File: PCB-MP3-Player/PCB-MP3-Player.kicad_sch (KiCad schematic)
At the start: 5 parts, among them J1 Conn_01x02_Pin, J2 PCM5102A, J3 Oled, J4 Conn_01x06_Pin

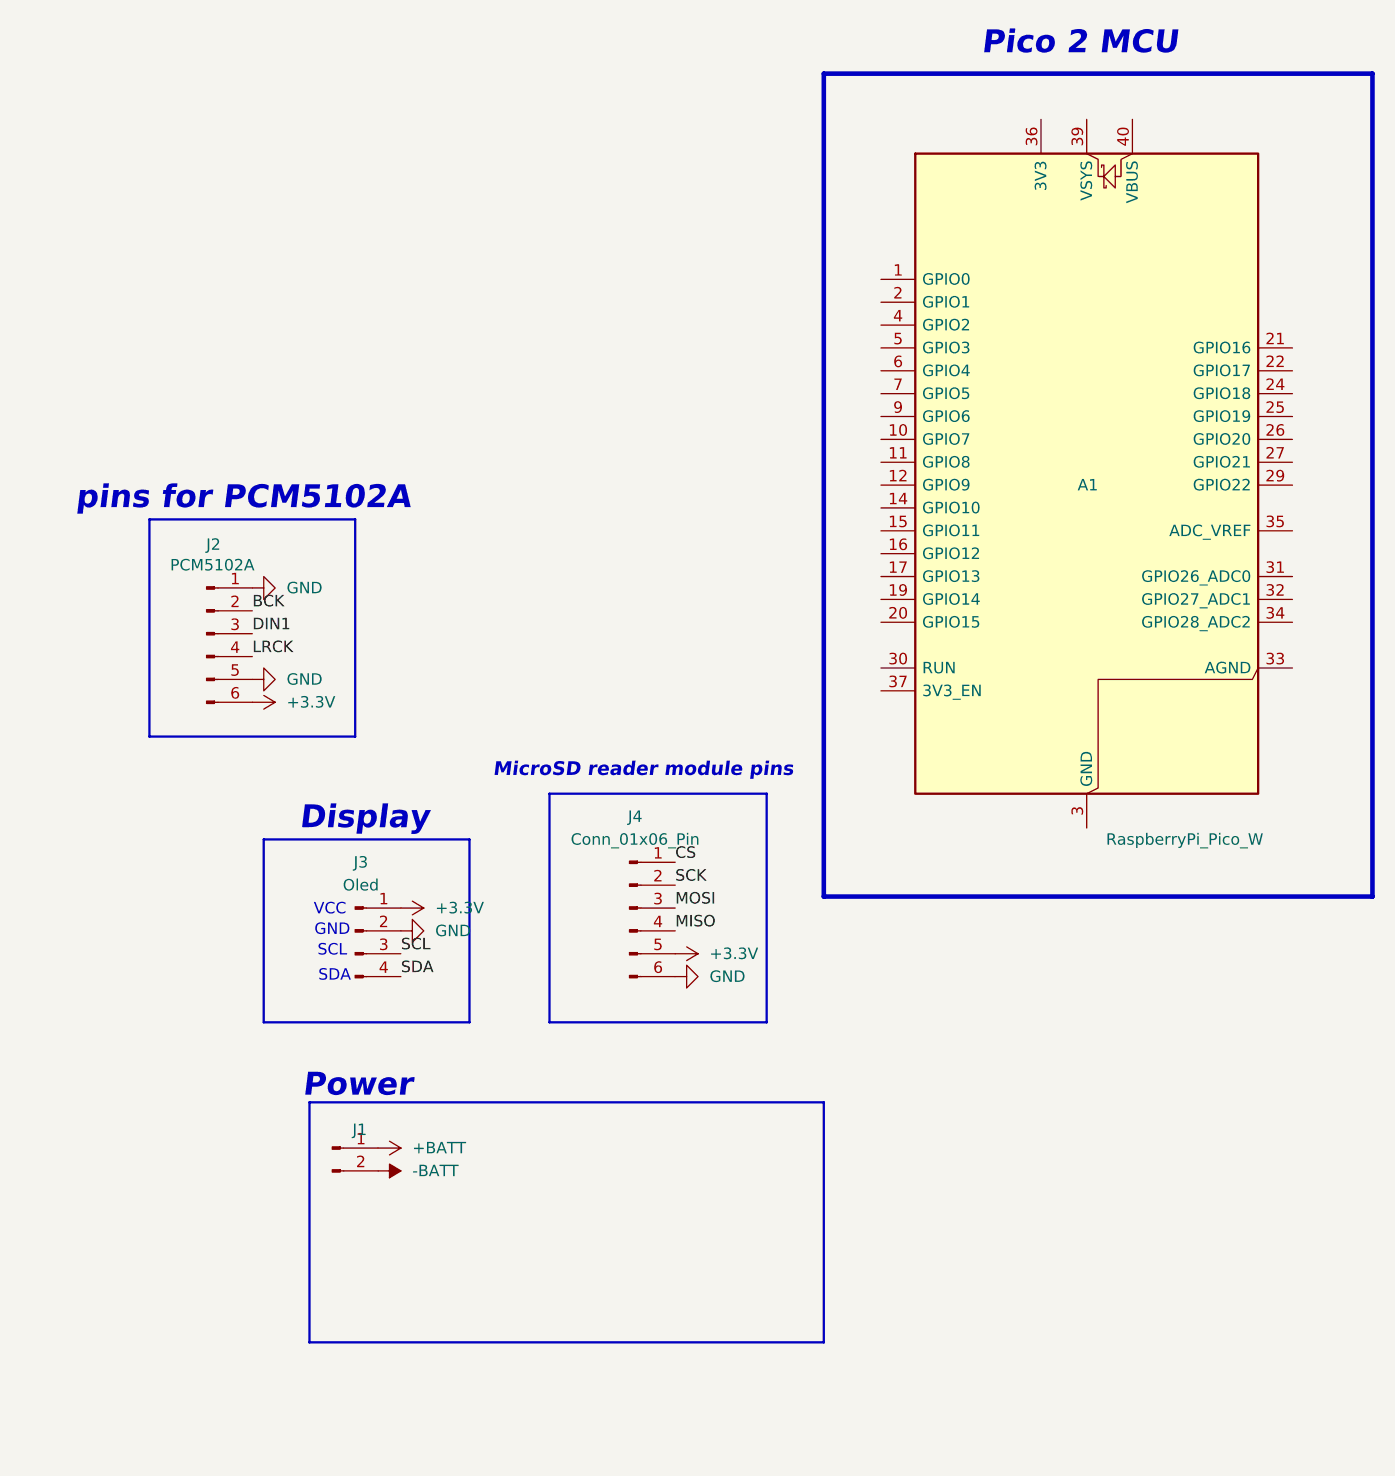
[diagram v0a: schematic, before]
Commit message: connected components together
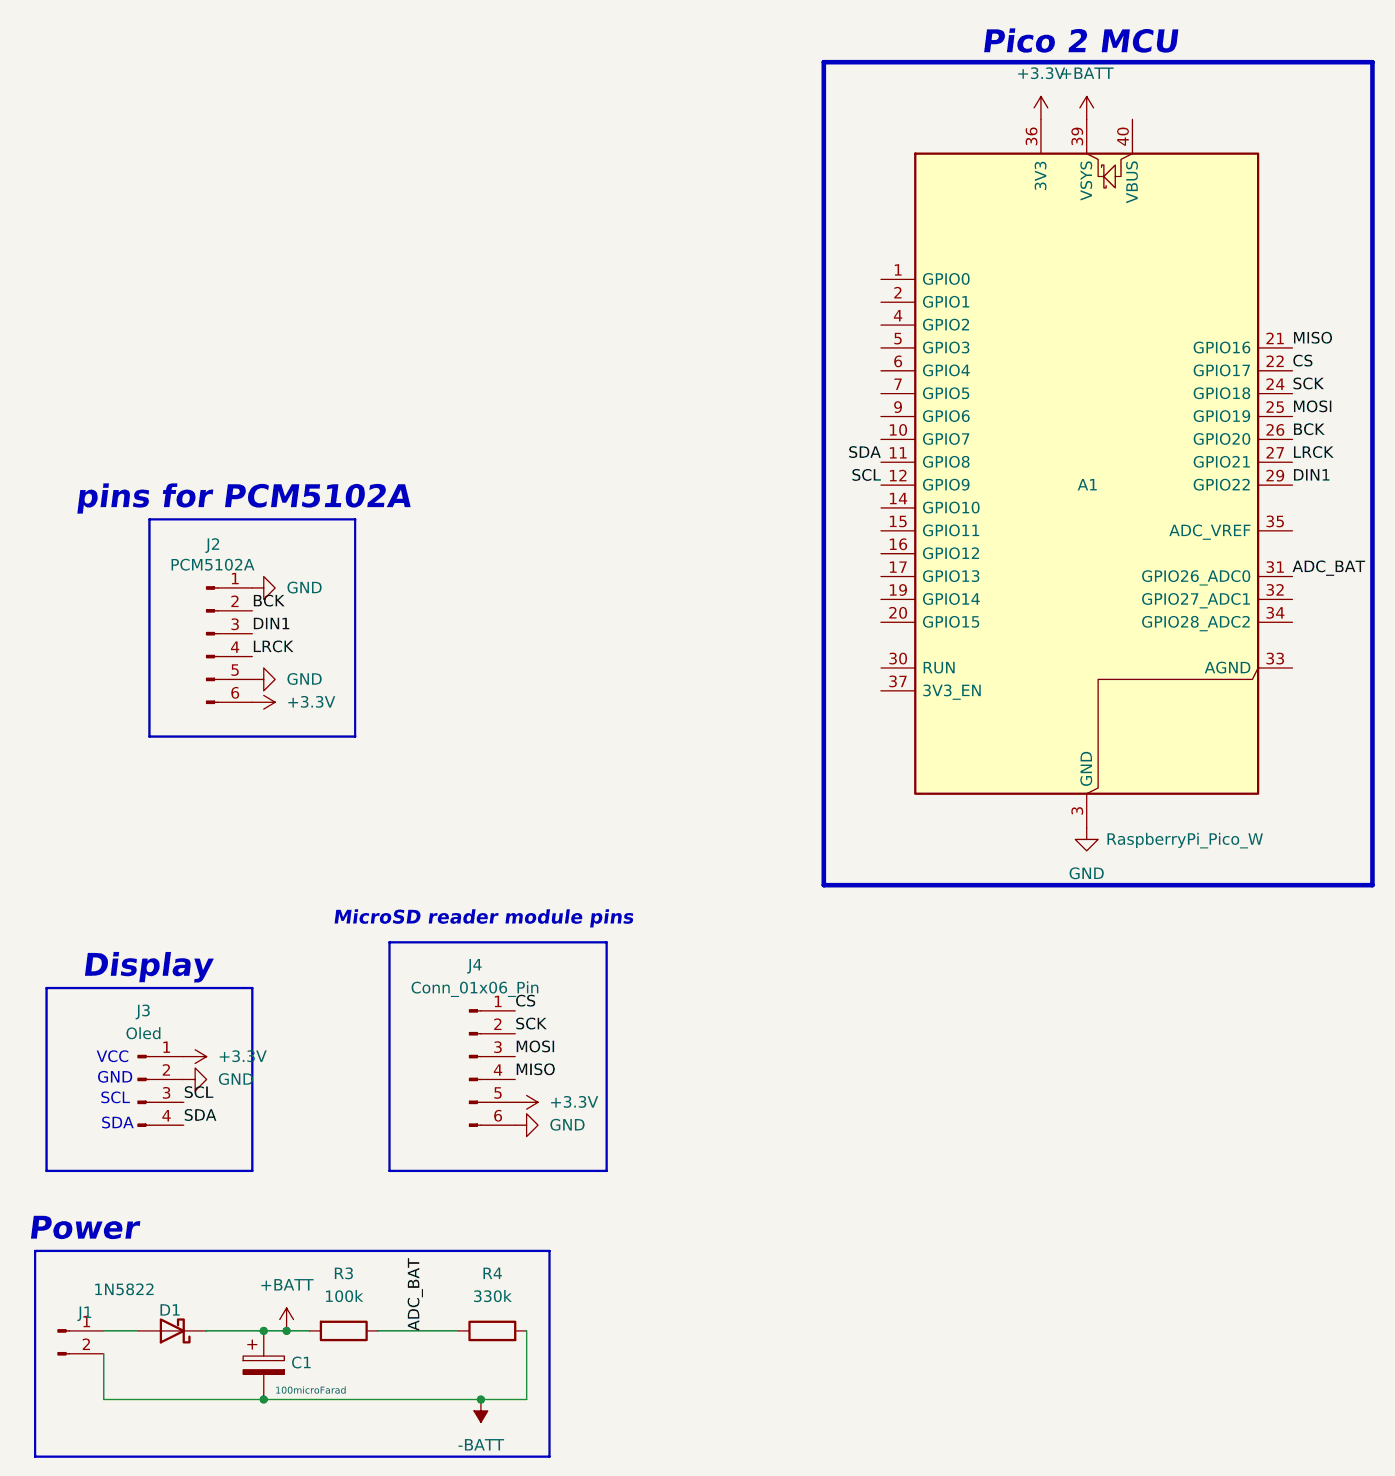
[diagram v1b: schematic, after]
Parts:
- added C1: 100microFarad, Capacitor_THT:CP_Radial_D6.3mm_P2.50mm, symbol Device:C_Polarized
- added D1: 1N5822, Diode_THT:D_DO-201AD_P15.24mm_Horizontal, symbol Device:D_Schottky
- added R3: 100k, Resistor_THT:R_Axial_DIN0207_L6.3mm_D2.5mm_P7.62mm_Horizontal, symbol Device:R
- added R4: 330k, Resistor_THT:R_Axial_DIN0207_L6.3mm_D2.5mm_P7.62mm_Horizontal, symbol Device:R
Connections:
- net +3.3V: now also A1.36 (3V3)
- net +BATT: now also A1.39 (VSYS), C1.1, D1.1 (K), R3.2; no longer J1.1 (Pin_1)
- net -BATT: now also C1.2, R4.2
- net BCK: now also A1.26 (GPIO20)
- net CS: now also A1.22 (GPIO17)
- net DIN1: now also A1.29 (GPIO22)
- net GND: now also A1.13 (GND), A1.18 (GND), A1.23 (GND), A1.28 (GND), A1.3 (GND), A1.38 (GND), A1.8 (GND)
- net LRCK: now also A1.27 (GPIO21)
- net MISO: now also A1.21 (GPIO16)
- net MOSI: now also A1.25 (GPIO19)
- net SCK: now also A1.24 (GPIO18)
- net SCL: now also A1.12 (GPIO9)
- net SDA: now also A1.11 (GPIO8)
- net ADC_BAT: now reaches A1.31 (GPIO26_ADC0)
- net ADC_BAT: now also R3.1, R4.1
- new net: D1.2 (A), J1.1 (Pin_1)
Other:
- moved on the sheet: J1, J3, J4
